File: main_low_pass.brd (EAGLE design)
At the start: 45.4 x 25.6 mm, 17 parts, among them IC1 74HC14D, X1 14867

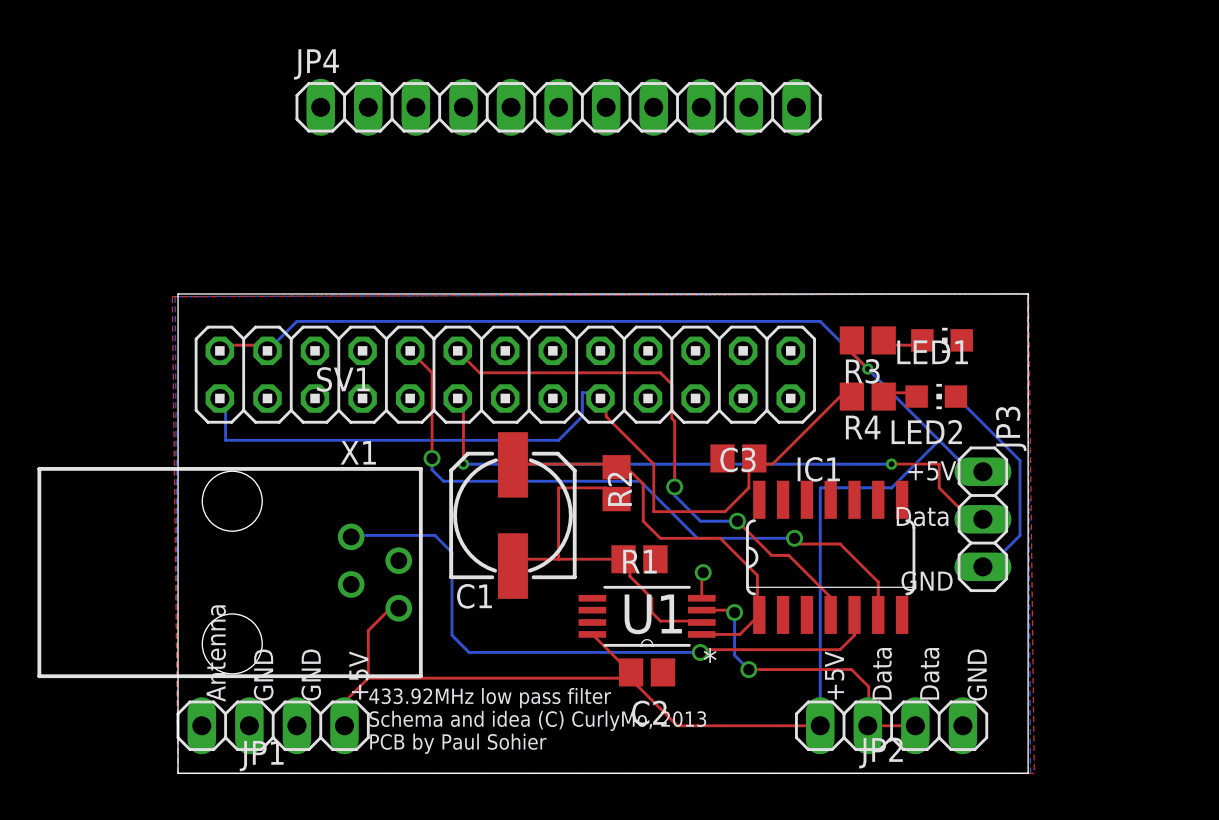
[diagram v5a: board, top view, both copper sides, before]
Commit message: Forgot a connection, removed outdated board files.
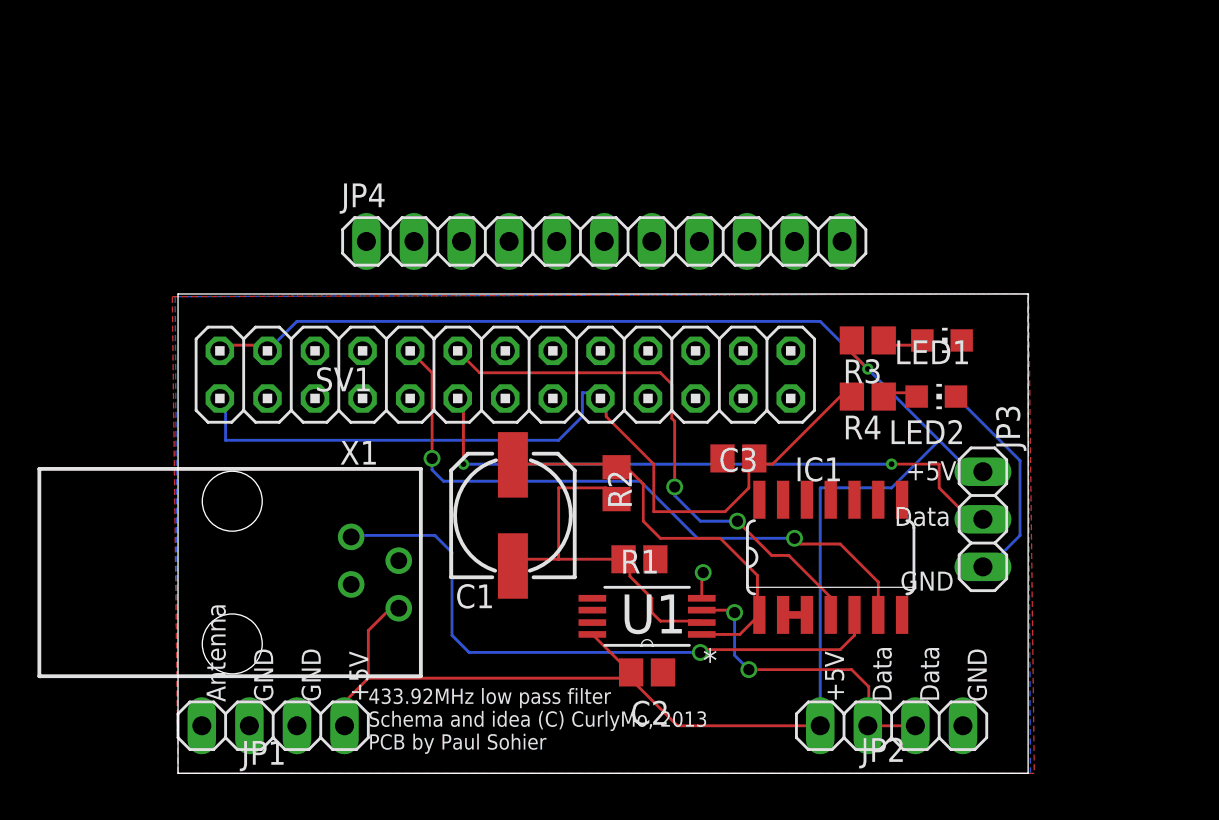
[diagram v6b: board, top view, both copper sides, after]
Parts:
- moved JP4 7.57 mm to (22.8, 27.1)
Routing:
- net N$3: track 0.00 -> 1.27 mm
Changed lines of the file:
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@@
 </element>
 <element name="R4" library="resistor" package="R0805" value="" x="36.83" y="18.8468" rot="R180"/>
-<element name="JP4" library="pinhead" package="1X11" value="" x="20.32" y="34.29"/>
+<element name="JP4" library="pinhead" package="1X11" value="" x="22.7584" y="27.1272"/>
 <element name="X1" library="con-4ucon" package="14867" value="14867" x="2.8956" y="9.4488" smashed="yes" rot="R270">
 <attribute name="OC_NEWARK" value="unknown" x="2.8956" y="9.4488" size="1.778" layer="27" rot="R270" display="off"/>
@@
 <contactref element="IC1" pad="2"/>
 <contactref element="IC1" pad="3"/>
-<wire x1="32.3088" y1="7.1882" x2="33.5788" y2="7.1882" width="0" layer="19" extent="1-1"/>
+<wire x1="32.3088" y1="7.1882" x2="33.5788" y2="7.1882" width="0.4064" layer="1"/>
 </signal>
 <signal name="N$7">
